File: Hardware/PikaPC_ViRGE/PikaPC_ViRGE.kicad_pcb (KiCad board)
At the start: 4 copper layers, 101.6 x 101.6 mm, 167 parts, among them J1 DIN41612_03x32_C_Split, J2 Conn_02x07_Odd_Even, J3 Conn_02x08_Odd_Even, J4 DE15_Socket_HighDensity_Mount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, U1 86C325, U10 74AHCT573, U12 74FCT2245, U13 74FCT2245, U14 74FCT2245, U15 74FCT2245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

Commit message: Prep for output
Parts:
- added R38: 147R, Resistor_SMD:R_0805_2012Metric, B.Cu at (99.1, 54.0)
- FB1, FB2, FB3: footprint Inductor_THT:L_Axial_L7.0mm_D3.3mm_P5.08mm_Vertical_Fastron_MICC -> Inductor_THT:L_Axial_L5.3mm_D2.2mm_P2.54mm_Vertical_Vishay_IM-1
- J4: footprint Connector_Dsub:DSUB-15-HD_Socket_Horizontal_P2.29x1.90mm_EdgePinOffset3.03mm_Housed_MountingHolesOffset4.94mm -> PikaPC_ViRGE:DE15 (EDAC 634-015)
- moved R8 10.3 mm to (95.2, 57.1), turned to 90 degrees
- moved J3 10.2 mm to (86.4, 47.0)
- moved FB3 9.67 mm to (90.2, 52.1)
- moved R9 9.61 mm to (92.7, 57.1), turned to 90 degrees
- moved R10 9.61 mm to (90.2, 57.1), turned to 90 degrees
- moved FB1 8.98 mm to (95.2, 52.1)
- moved FB2 8.98 mm to (92.7, 52.1)
- moved J4 5.99 mm to (99.7, 25.4)
- moved R16 3.59 mm to (101.6, 55.9), turned to 180 degrees
- turned R17 to 180 degrees
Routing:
- net /Video/Vid-H: track 86.2 -> 36.9 mm, vias 0 -> 1
- net /Video/Vid-V: track 78.8 -> 31.9 mm, vias 0 -> 1
- net /Video/Vid-B: track 29.1 -> 20.2 mm
- net /Video/Vid-G: track 25.3 -> 17.4 mm
- net /Video/Vid-R: track 21.8 -> 15.0 mm
- net /Video/Vid-G-Out: track 31.2 -> 24.8 mm
- net /Video/Vid-R-Out: track 22.6 -> 27.2 mm
- net /Video/Vid-B-Out: track 25.3 -> 20.9 mm
- net /Main Bus/~{Bus-BE2}: track 57.0 -> 53.0 mm
- net /Power/RSET: track 5.62 -> 8.20 mm
- net /VRAM/~{VMCAS0}: track 21.1 -> 18.9 mm
- net /Main Bus/~{Bus-BE3}: track 46.1 -> 44.0 mm
- net /Video/VidClk: track 23.0 -> 21.2 mm
- net /VRAM/~{VMCAS1}: track 21.9 -> 20.1 mm
- net /VRAM/~{VMCAS2}: track 22.0 -> 20.2 mm
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
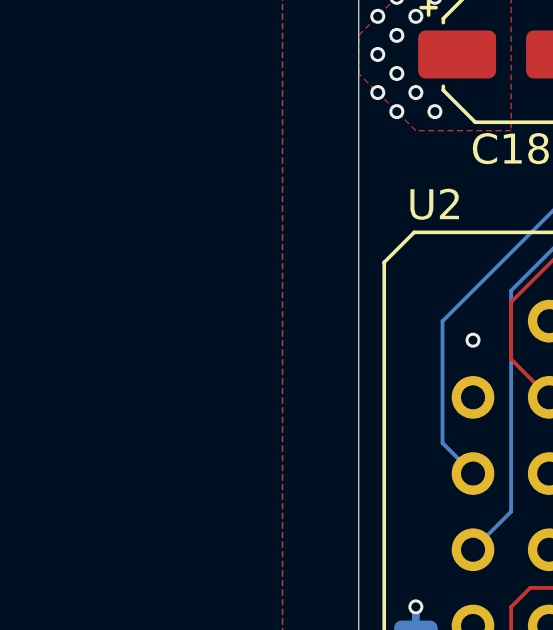
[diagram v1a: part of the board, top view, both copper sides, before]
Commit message: add missing pull-ups on SRDY# & RDYIN#
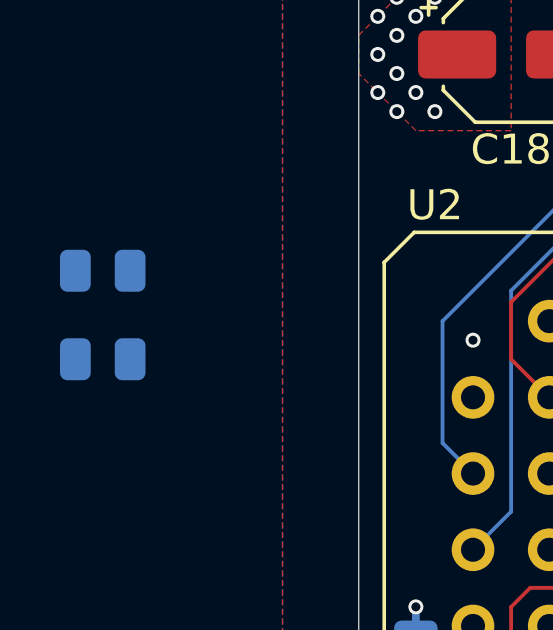
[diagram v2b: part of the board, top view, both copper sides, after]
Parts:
- added R39: 10K, Resistor_SMD:R_0805_2012Metric, B.Cu at (67.7, 73.7)
- added R40: 10K, Resistor_SMD:R_0805_2012Metric, B.Cu at (67.7, 70.7)
